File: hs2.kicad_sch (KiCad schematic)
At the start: 89 parts, among them J1 Conn_01x01, J2 Conn_01x01, J3 Conn_01x02, J4 Conn_01x01, J5 Conn_01x01, Q1 2N5457, Q2 2N3904, Q3 2N3906, Q4 2N3904, U1 Opamp_Dual, U2 Opamp_Dual, U3 Opamp_Dual

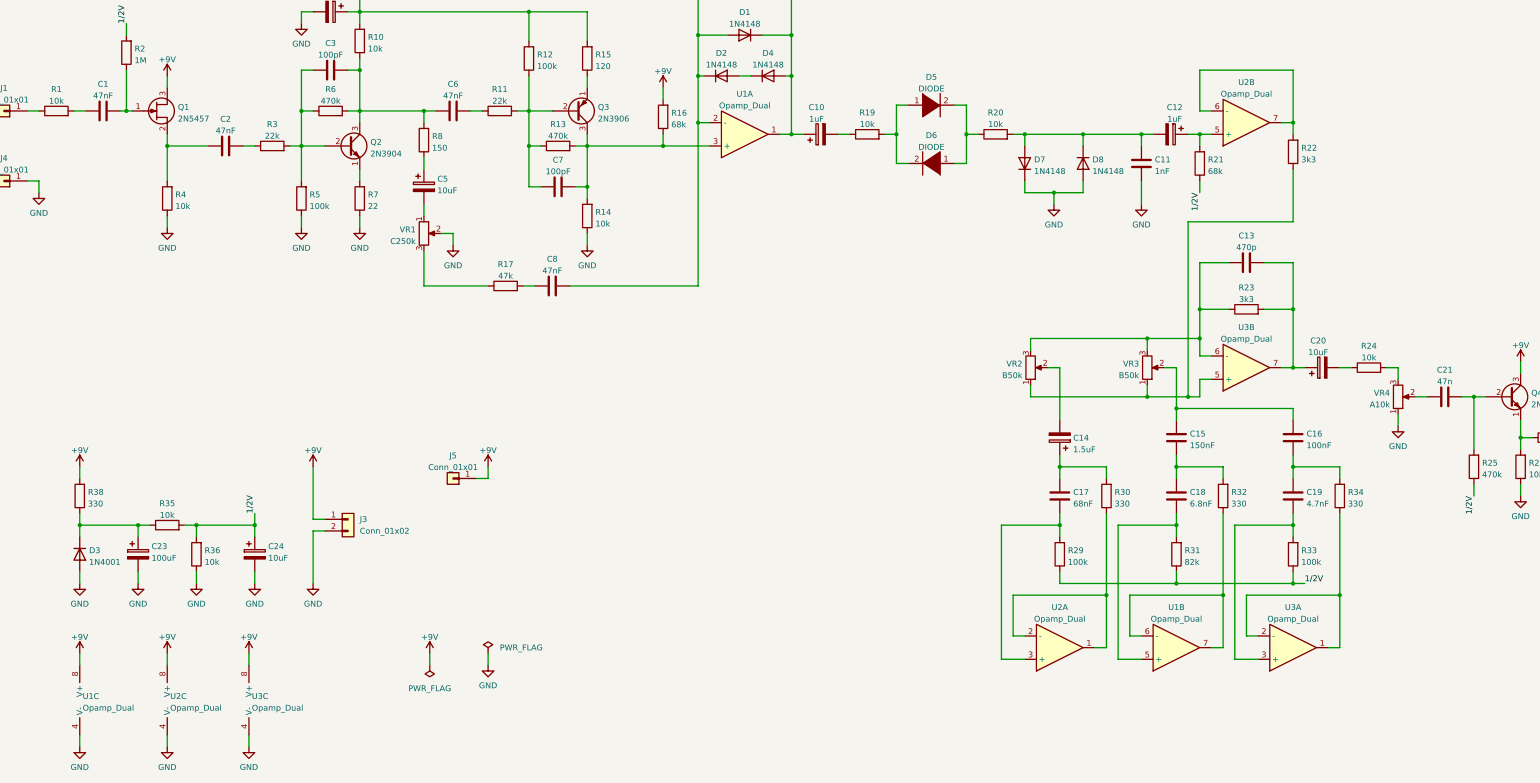
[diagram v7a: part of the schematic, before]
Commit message: Minor fixes in the schematics
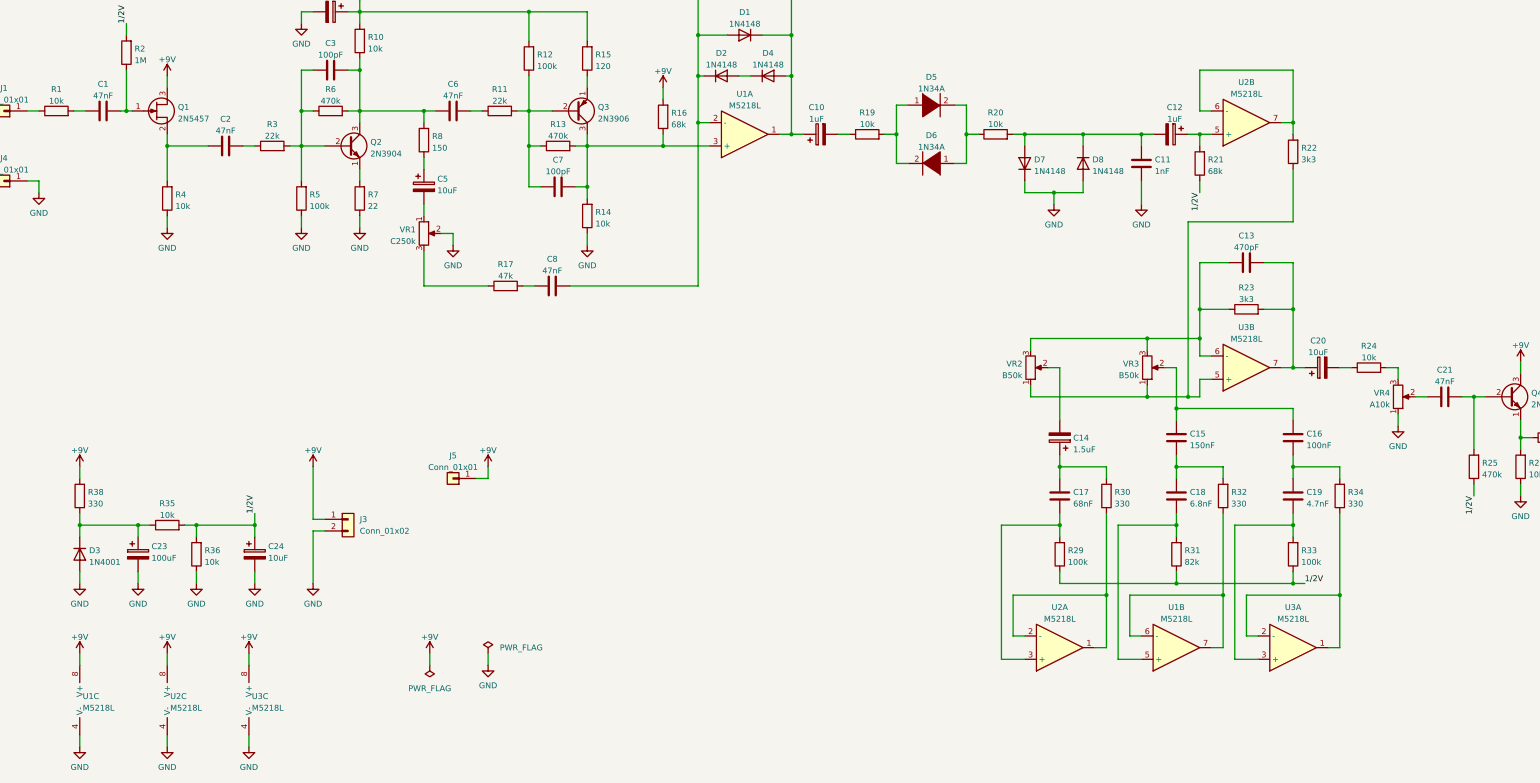
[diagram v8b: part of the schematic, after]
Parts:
- C13: value 470p -> 470pF
- C21: value 47n -> 47nF
- D5, D6: value DIODE -> 1N34A
- U1, U2, U3: value Opamp_Dual -> M5218L
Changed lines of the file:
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@@
     (in_bom yes) (on_board yes) (fields_autoplaced)
     (property "Reference" "C21" (id 0) (at 335.28 154.1612 90))
-    (property "Value" "47n" (id 1) (at 335.28 156.6981 90))
+    (property "Value" "47nF" (id 1) (at 335.28 156.6981 90))
     (property "Footprint" "Capacitor_THT:C_Disc_D4.3mm_W1.9mm_P5.00mm" (id 2) (at 339.09 159.0548 0)
       (effects (font (size 1.27 1.27)) hide)
@@
     (in_bom yes) (on_board yes) (fields_autoplaced)
     (property "Reference" "U3" (id 0) (at 292.1 144.8902 0))
-    (property "Value" "Opamp_Dual" (id 1) (at 292.1 147.4271 0))
+    (property "Value" "M5218L" (id 1) (at 292.1 147.4271 0))
     (property "Footprint" "Package_SIP:SIP-8_19x3mm_P2.54mm" (id 2) (at 292.1 153.67 0)
       (effects (font (size 1.27 1.27)) hide)
@@
     (in_bom yes) (on_board yes) (fields_autoplaced)
     (property "Reference" "U2" (id 0) (at 251.46 205.8502 0))
-    (property "Value" "Opamp_Dual" (id 1) (at 251.46 208.3871 0))
+    (property "Value" "M5218L" (id 1) (at 251.46 208.3871 0))
     (property "Footprint" "Package_SIP:SIP-8_19x3mm_P2.54mm" (id 2) (at 251.46 214.63 0)
       (effects (font (size 1.27 1.27)) hide)
@@
     (in_bom yes) (on_board yes) (fields_autoplaced)
     (property "Reference" "C13" (id 0) (at 292.1 124.9512 90))
-    (property "Value" "470p" (id 1) (at 292.1 127.4881 90))
+    (property "Value" "470pF" (id 1) (at 292.1 127.4881 90))
     (property "Footprint" "Capacitor_THT:C_Disc_D4.3mm_W1.9mm_P5.00mm" (id 2) (at 295.91 129.8448 0)
       (effects (font (size 1.27 1.27)) hide)
@@
     (in_bom yes) (on_board yes) (fields_autoplaced)
     (property "Reference" "U1" (id 0) (at 182.88 94.0902 0))
-    (property "Value" "Opamp_Dual" (id 1) (at 182.88 96.6271 0))
+    (property "Value" "M5218L" (id 1) (at 182.88 96.6271 0))
     (property "Footprint" "Package_SIP:SIP-8_19x3mm_P2.54mm" (id 2) (at 182.88 102.87 0)
       (effects (font (size 1.27 1.27)) hide)
@@
     (in_bom yes) (on_board yes) (fields_autoplaced)
     (property "Reference" "U3" (id 0) (at 302.26 205.8502 0))
-    (property "Value" "Opamp_Dual" (id 1) (at 302.26 208.3871 0))
+    (property "Value" "M5218L" (id 1) (at 302.26 208.3871 0))
     (property "Footprint" "Package_SIP:SIP-8_19x3mm_P2.54mm" (id 2) (at 302.26 214.63 0)
       (effects (font (size 1.27 1.27)) hide)
@@
     (in_bom yes) (on_board yes) (fields_autoplaced)
     (property "Reference" "U2" (id 0) (at 292.1 91.5502 0))
-    (property "Value" "Opamp_Dual" (id 1) (at 292.1 94.0871 0))
+    (property "Value" "M5218L" (id 1) (at 292.1 94.0871 0))
     (property "Footprint" "Package_SIP:SIP-8_19x3mm_P2.54mm" (id 2) (at 292.1 100.33 0)
       (effects (font (size 1.27 1.27)) hide)
@@
     (in_bom yes) (on_board yes) (fields_autoplaced)
     (property "Reference" "D5" (id 0) (at 223.52 90.4072 0))
-    (property "Value" "DIODE" (id 1) (at 223.52 92.9441 0))
+    (property "Value" "1N34A" (id 1) (at 223.52 92.9441 0))
     (property "Footprint" "Diode_THT:D_DO-41_SOD81_P10.16mm_Horizontal" (id 2) (at 223.52 96.52 0)
       (effects (font (size 1.27 1.27)) hide)
@@
       (effects (font (size 1.27 1.27)) (justify left))
     )
-    (property "Value" "Opamp_Dual" (id 1) (at 75.565 227.7622 0)
+    (property "Value" "M5218L" (id 1) (at 75.565 227.7622 0)
       (effects (font (size 1.27 1.27)) (justify left))
     )
@@
     (in_bom yes) (on_board yes) (fields_autoplaced)
     (property "Reference" "D6" (id 0) (at 223.52 103.1072 0))
-    (property "Value" "DIODE" (id 1) (at 223.52 105.6441 0))
+    (property "Value" "1N34A" (id 1) (at 223.52 105.6441 0))
     (property "Footprint" "Diode_THT:D_DO-41_SOD81_P10.16mm_Horizontal" (id 2) (at 223.52 109.22 0)
       (effects (font (size 1.27 1.27)) hide)
@@
     (in_bom yes) (on_board yes) (fields_autoplaced)
     (property "Reference" "U1" (id 0) (at 276.86 205.8502 0))
-    (property "Value" "Opamp_Dual" (id 1) (at 276.86 208.3871 0))
+    (property "Value" "M5218L" (id 1) (at 276.86 208.3871 0))
     (property "Footprint" "Package_SIP:SIP-8_19x3mm_P2.54mm" (id 2) (at 276.86 214.63 0)
       (effects (font (size 1.27 1.27)) hide)
@@
       (effects (font (size 1.27 1.27)) (justify left))
     )
-    (property "Value" "Opamp_Dual" (id 1) (at 38.735 227.7622 0)
+    (property "Value" "M5218L" (id 1) (at 38.735 227.7622 0)
       (effects (font (size 1.27 1.27)) (justify left))
     )
@@
       (effects (font (size 1.27 1.27)) (justify left))
     )
-    (property "Value" "Opamp_Dual" (id 1) (at 57.785 227.7622 0)
+    (property "Value" "M5218L" (id 1) (at 57.785 227.7622 0)
       (effects (font (size 1.27 1.27)) (justify left))
     )
@@
     )
     (path "/4b3a3982-621e-4ca4-9fa4-c5bd301a6833"
-      (reference "C13") (unit 1) (value "470p") (footprint "Capacitor_THT:C_Disc_D4.3mm_W1.9mm_P5.00mm")
+      (reference "C13") (unit 1) (value "470pF") (footprint "Capacitor_THT:C_Disc_D4.3mm_W1.9mm_P5.00mm")
     )
     (path "/e4c012e0-9f8a-453f-96ce-77ccb376a2fb"
@@
     )
     (path "/02bc8548-a693-40bd-b6d3-47be4eaf491a"
-      (reference "C21") (unit 1) (value "47n") (footprint "Capacitor_THT:C_Disc_D4.3mm_W1.9mm_P5.00mm")
+      (reference "C21") (unit 1) (value "47nF") (footprint "Capacitor_THT:C_Disc_D4.3mm_W1.9mm_P5.00mm")
     )
     (path "/059bcad1-2eec-4327-8b5c-f06a4c26300e"
@@
     )
     (path "/b75a61a3-6d3e-4cff-b4d0-4d104ceeabfb"
-      (reference "D5") (unit 1) (value "DIODE") (footprint "Diode_THT:D_DO-41_SOD81_P10.16mm_Horizontal")
+      (reference "D5") (unit 1) (value "1N34A") (footprint "Diode_THT:D_DO-41_SOD81_P10.16mm_Horizontal")
     )
     (path "/c4083a00-b7b8-474b-aa21-f3ada39690d0"
-      (reference "D6") (unit 1) (value "DIODE") (footprint "Diode_THT:D_DO-41_SOD81_P10.16mm_Horizontal")
+      (reference "D6") (unit 1) (value "1N34A") (footprint "Diode_THT:D_DO-41_SOD81_P10.16mm_Horizontal")
     )
     (path "/df4c3e85-8b2c-473a-906c-59f41b9a1adf"
@@
     )
     (path "/4fbc4693-bd7e-4f8c-a936-ef7107a97c74"
-      (reference "U1") (unit 1) (value "Opamp_Dual") (footprint "Package_SIP:SIP-8_19x3mm_P2.54mm")
+      (reference "U1") (unit 1) (value "M5218L") (footprint "Package_SIP:SIP-8_19x3mm_P2.54mm")
     )
     (path "/e4cffc74-63ba-4281-8119-8993ba0d290a"
-      (reference "U1") (unit 2) (value "Opamp_Dual") (footprint "Package_SIP:SIP-8_19x3mm_P2.54mm")
+      (reference "U1") (unit 2) (value "M5218L") (footprint "Package_SIP:SIP-8_19x3mm_P2.54mm")
     )
     (path "/e69ceb0f-9881-484a-9949-dc7f1ddc4e1d"
-      (reference "U1") (unit 3) (value "Opamp_Dual") (footprint "Package_SIP:SIP-8_19x3mm_P2.54mm")
+      (reference "U1") (unit 3) (value "M5218L") (footprint "Package_SIP:SIP-8_19x3mm_P2.54mm")
     )
     (path "/28db9cb7-58df-4094-8e40-cd1fa8991d0a"
-      (reference "U2") (unit 1) (value "Opamp_Dual") (footprint "Package_SIP:SIP-8_19x3mm_P2.54mm")
+      (reference "U2") (unit 1) (value "M5218L") (footprint "Package_SIP:SIP-8_19x3mm_P2.54mm")
     )
     (path "/b0d654ba-fccb-4228-9b7e-d1ed9894ae9f"
-      (reference "U2") (unit 2) (value "Opamp_Dual") (footprint "Package_SIP:SIP-8_19x3mm_P2.54mm")
+      (reference "U2") (unit 2) (value "M5218L") (footprint "Package_SIP:SIP-8_19x3mm_P2.54mm")
     )
     (path "/ef3ed138-1b04-4b13-8d9d-b9c73b0d72a2"
-      (reference "U2") (unit 3) (value "Opamp_Dual") (footprint "Package_SIP:SIP-8_19x3mm_P2.54mm")
+      (reference "U2") (unit 3) (value "M5218L") (footprint "Package_SIP:SIP-8_19x3mm_P2.54mm")
     )
     (path "/a02895ff-9a0a-4603-be35-1034c3ff6b40"
-      (reference "U3") (unit 1) (value "Opamp_Dual") (footprint "Package_SIP:SIP-8_19x3mm_P2.54mm")
+      (reference "U3") (unit 1) (value "M5218L") (footprint "Package_SIP:SIP-8_19x3mm_P2.54mm")
     )
     (path "/0c451c3b-50f4-4244-b981-fa5436ed2266"
-      (reference "U3") (unit 2) (value "Opamp_Dual") (footprint "Package_SIP:SIP-8_19x3mm_P2.54mm")
+      (reference "U3") (unit 2) (value "M5218L") (footprint "Package_SIP:SIP-8_19x3mm_P2.54mm")
     )
     (path "/b8fdacbb-fb36-47ff-8dbb-4ca2741d4e0f"
-      (reference "U3") (unit 3) (value "Opamp_Dual") (footprint "Package_SIP:SIP-8_19x3mm_P2.54mm")
+      (reference "U3") (unit 3) (value "M5218L") (footprint "Package_SIP:SIP-8_19x3mm_P2.54mm")
     )
     (path "/a427a193-8090-4a2e-b22b-102943c60dd4"
